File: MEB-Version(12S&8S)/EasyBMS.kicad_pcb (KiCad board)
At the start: 2 copper layers, 48.8 x 100 mm, 174 parts, among them IC1 XL7046, IC2 LTC6811IG-1#PBF, IC3 ISO1042DWV, IC4 AMS1117-3.3, J1 TYPE-C-31-M-12, Q14 CJ2301, Q15 CJ2301, Q16 CJ2301, Q18 CJ2301, Q20 CJ2301, Q22 CJ2301, Q24 CJ2301, Q26 CJ2301, Q28 CJ2301, Q30 CJ2301, Q32 CJ2301, Q34 CJ2301, U1 ESP32-C6-MINI-1-N4, Y1 FC-135_32.7680KA-A5

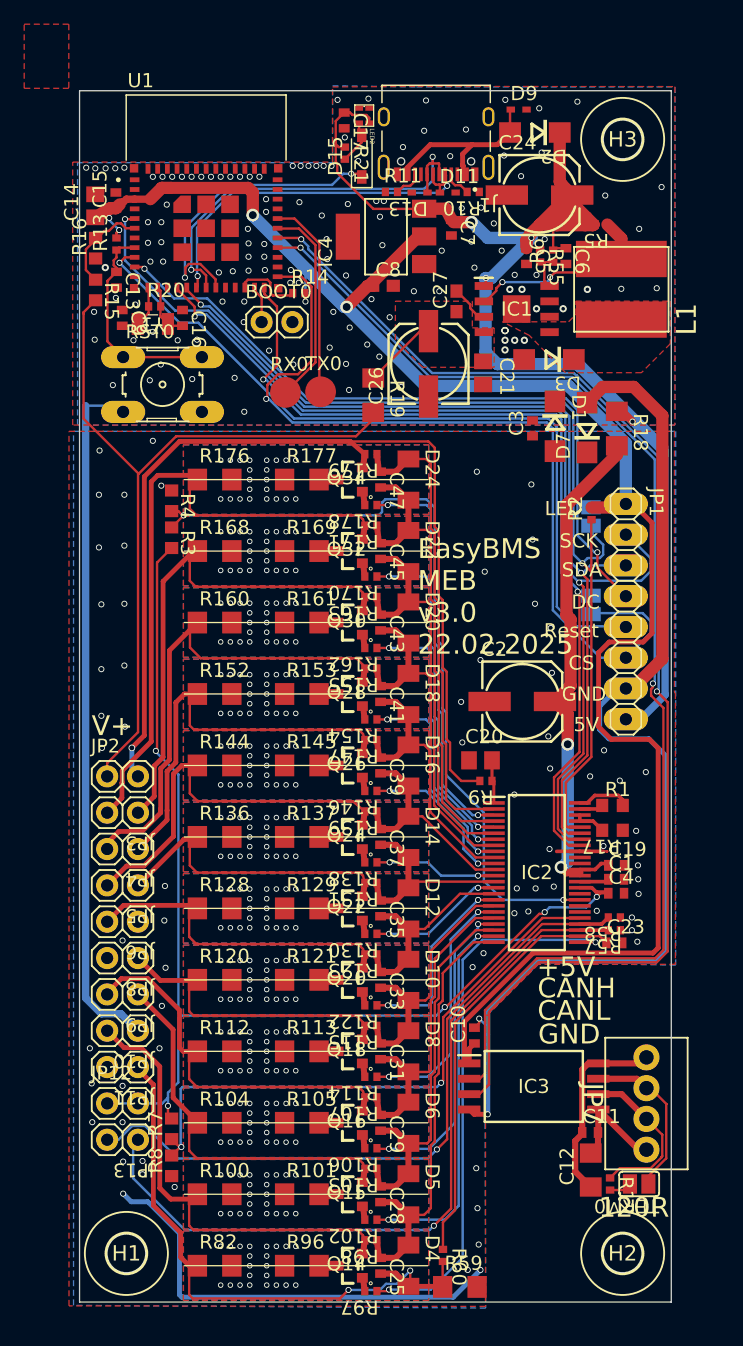
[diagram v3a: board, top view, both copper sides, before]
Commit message: new grounding with one common ground
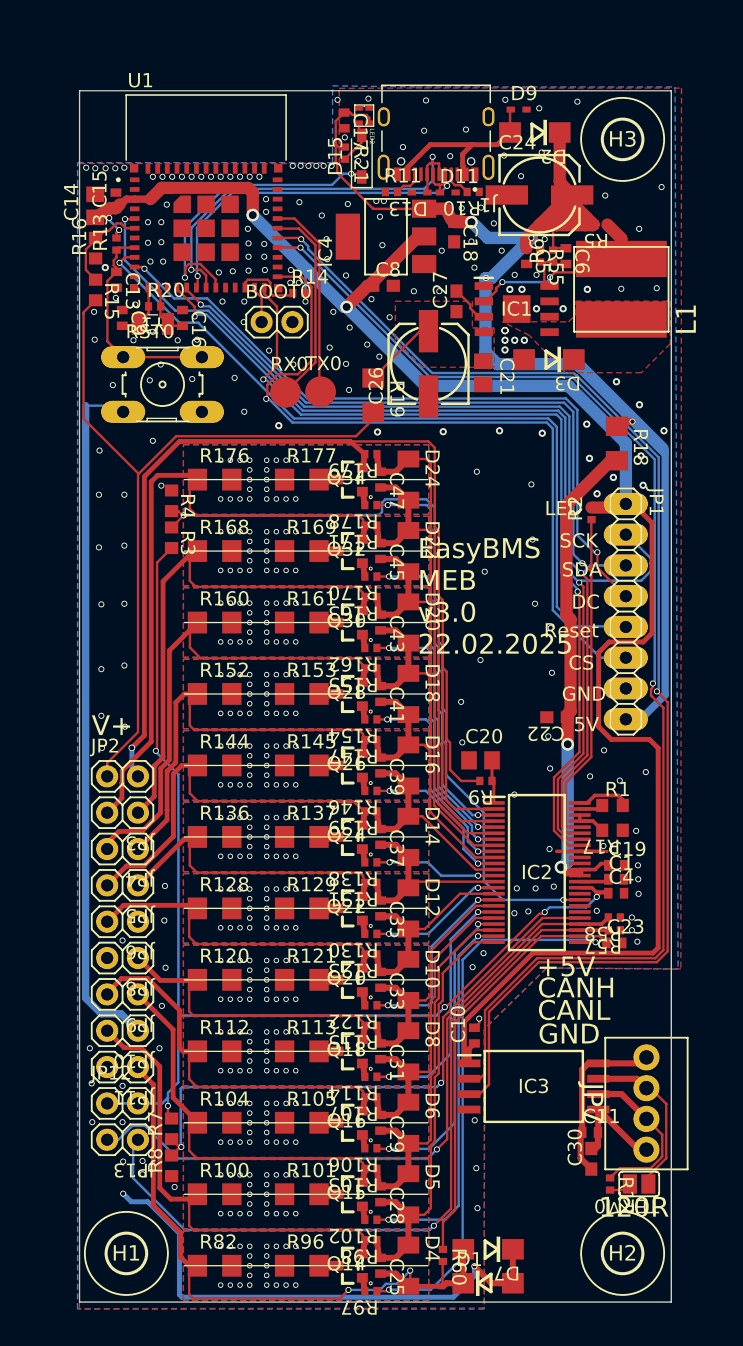
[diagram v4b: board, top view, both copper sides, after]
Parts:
- removed C12: 47µF, EasyBMS:C1206_334
- removed C2: 100µF/16V, EasyBMS:153CLV-0605_334
- removed C3: 100nF, EasyBMS:C0402_334
- removed C7: 1uF, EasyBMS:C0402_334
- removed CSLTC0, MISO0: SJ, EasyBMS:SJ_252
- removed R59: 600R@100MHz, EasyBMS:R1206_334
- added C18: 22uF, EasyBMS:C0603_334, F.Cu at (155.0, 66.6)
- added C22: 22uF, EasyBMS:C0603_334, F.Cu at (163.5, 106.7)
- added C30: 22uF, EasyBMS:C0603_334, F.Cu at (166.3, 143.2)
- moved D1 71.0 mm to (157.8, 153.4), turned to 0 degrees
- moved D7 68.3 mm to (157.8, 150.7), turned to 180 degrees
- moved R18 1.23 mm to (168.4, 84.1)
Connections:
- C1 pad 2: /GND2 -> GND
- C19 pad 2: /GND2 -> GND
- C20 pad 1: /GND2 -> GND
- C23 pad 2: /GND2 -> GND
- C4 pad 2: /GND2 -> GND
- D1 pad A: /GND2 -> GND
- D1 pad C: GND -> /C1-
- D7 pad A: GND -> /C1-
- D7 pad C: /GND2 -> GND
- IC2 pad 30: /GND2 -> GND
- IC2 pad 31: /GND2 -> GND
- IC2 pad 40: /GND2 -> GND
- R17 pad 1: /GND2 -> GND
- R4 pad 1: /GND2 -> GND
- R57 pad 1: /GND2 -> GND
- R58 pad 1: /GND2 -> GND
- R8 pad 1: /GND2 -> GND
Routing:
- net /GND2: track 41.1 -> 0.00 mm, vias 69 -> 0
- net GND: track 146.5 -> 108.4 mm, vias 129 -> 209
- net /CSDSPL: track 71.4 -> 62.3 mm
- net /C1-: track 49.8 -> 54.7 mm
- net /MISO: track 82.3 -> 77.5 mm
- net +5V: track 42.7 -> 40.9 mm
- net Net-(IC3-VCC2): track 16.2 -> 14.5 mm
- net /A0DSPL: track 60.0 -> 58.6 mm
- net /CSLTC: track 73.9 -> 72.6 mm
- net +5V/1: track 112.5 -> 112.2 mm, vias 4 -> 5
- removed copper zone on B.Cu, net /GND2
- removed copper zone on F.Cu, net /GND2

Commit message: add ESD protection to CAN, more clearance on high voltage diff
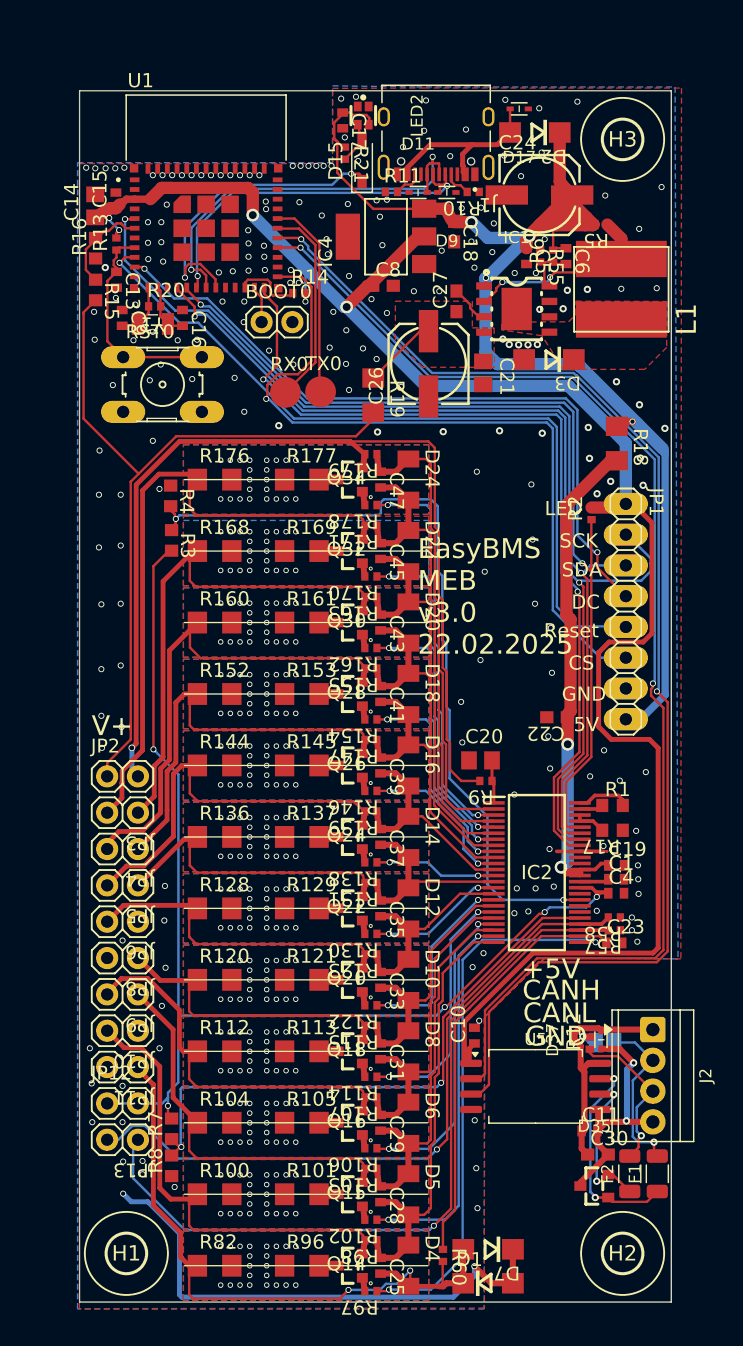
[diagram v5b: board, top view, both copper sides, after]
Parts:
- removed D13: LESD5D5.0CT1G, EasyBMS:SOD523_210
- removed IC3: ISO1042DWV, EasyBMS:SOIC127P1150X280-8N
- removed JP7: 2828XX-4282834-4, EasyBMS:TERMBLK_254-4N_16378166
- added D17: LESD5D5.0CT1G_C5199850, EasyEDA2KiCAD:SOD-523_L1.2-W0.8-LS1.6-BI, F.Cu at (160.4, 56.5)
- added D35: PESD1CAN,215, EasyEDA2KiCAD:SOT-23_L2.9-W1.3-P1.90-LS2.4-BR, F.Cu at (166.6, 145.4)
- added D37: LESD5D5.0CT1G_C5199850, EasyEDA2KiCAD:SOD-523_L1.2-W0.8-LS1.6-BI, F.Cu at (167.1, 133.3)
- added F1: 60V 100mA/JK-NSMD010, Resistor_SMD:R_1206_3216Metric, F.Cu at (171.8, 144.4)
- added F2: 60V 100mA/JK-NSMD010, Resistor_SMD:R_1206_3216Metric, F.Cu at (169.5, 144.4)
- added J2: Screw_Terminal_01x04, TerminalBlock_TE-Connectivity:TerminalBlock_TE_282834-4_1x04_P2.54mm_Horizontal, F.Cu at (171.4, 132.5)
- added U5: CA-IS3050CG, Package_SO:SOIC-8_7.5x5.85mm_P1.27mm, F.Cu at (161.7, 137.2)
- D11, D9: value LESD5D5.0CT1G -> LESD5D5.0CT1G_C5199850; footprint EasyBMS:SOD523_210 -> EasyEDA2KiCAD:SOD-523_L1.2-W0.8-LS1.6-BI
- IC1: footprint EasyBMS:SOIC127P600X170-9N -> EasyEDA2KiCAD:ESOP-8_L4.9-W3.9-P1.27-LS6.0-TL-EP
- LED2: footprint EasyBMS:XL-1615RGBC-WS2812B -> EasyEDA2KiCAD:LED-SMD_4P-L1.6-W1.5_XL-1615RGBC-WS2812B-1
- TERM0: moved to B.Cu
- moved TERM0 12.0 mm to (167.5, 133.6)
- moved R12 11.7 mm to (166.2, 133.6), turned to 90 degrees
- moved D9 9.02 mm to (154.4, 63.4), turned to 180 degrees
- moved D11 2.40 mm to (152.0, 63.4)
- moved C30 0.65 mm to (166.9, 142.8), turned to 0 degrees
- moved R4 0.41 mm to (131.6, 88.5)
- moved D15 0.39 mm to (147.4, 60.8)
- moved R3 0.22 mm to (131.7, 92.1)
- moved C11 0.14 mm to (166.2, 140.9)
- moved C17 0.13 mm to (145.8, 57.5)
- moved LED2 0.08 mm to (147.5, 57.1)
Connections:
- D2 pad A: Net-(D2-PadA) -> Net-(D17-Pad2)
- J1 pad A4_B9: Net-(D2-PadA) -> Net-(D17-Pad2)
- J1 pad B4_A9: Net-(D2-PadA) -> Net-(D17-Pad2)
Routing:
- net GND: track 108.4 -> 51.3 mm, vias 209 -> 208
- net Net-(U5-CANH): track 0.00 -> 17.6 mm, vias 0 -> 2
- net Net-(D2-PadA): track 15.0 -> 0.00 mm
- net Net-(D17-Pad2): track 0.00 -> 15.0 mm
- net Net-(U5-CANL): track 0.00 -> 12.4 mm, vias 0 -> 2
- net Net-(J2-Pin_4): track 9.02 -> 20.9 mm, vias 0 -> 2
- net Net-(J2-Pin_1): track 14.5 -> 19.4 mm
- net /VTEMPNORTH: track 65.7 -> 66.7 mm
- net Net-(R12-Pad2): track 1.85 -> 2.70 mm, vias 0 -> 1
- net Net-(J2-Pin_2): track 13.7 -> 14.2 mm, vias 0 -> 1
- net +5V/1: track 112.2 -> 111.7 mm, vias 5 -> 4
- net Net-(J2-Pin_3): track 13.5 -> 13.3 mm, vias 0 -> 1

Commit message: changed settings for jlc parts
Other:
- board text added: "EasyBMS MEB v3.1 19.05.2025"
- board text removed: "EasyBMS MEB v3.0 22.02.2025"
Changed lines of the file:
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@@
 		(sheetname "/")
 		(sheetfile "EasyBMS.kicad_sch")
-		(attr exclude_from_bom)
+		(attr exclude_from_pos_files exclude_from_bom)
 		(fp_poly
 			(pts
@@
 		(sheetname "/")
 		(sheetfile "EasyBMS.kicad_sch")
+		(attr exclude_from_pos_files exclude_from_bom)
 		(fp_line
 			(start 2.54 0.635)
@@
 		(sheetname "/")
 		(sheetfile "EasyBMS.kicad_sch")
-		(attr exclude_from_bom)
+		(attr exclude_from_pos_files exclude_from_bom)
 		(fp_poly
 			(pts
@@
 		(sheetname "/")
 		(sheetfile "EasyBMS.kicad_sch")
-		(attr exclude_from_bom)
+		(attr exclude_from_pos_files exclude_from_bom)
 		(fp_poly
 			(pts
@@
 		(sheetname "/")
 		(sheetfile "EasyBMS.kicad_sch")
-		(attr exclude_from_bom)
+		(attr exclude_from_pos_files exclude_from_bom)
 		(fp_poly
 			(pts
@@
 		(sheetname "/")
 		(sheetfile "EasyBMS.kicad_sch")
+		(attr exclude_from_pos_files exclude_from_bom)
 		(fp_line
 			(start 2.54 0.635)
@@
 		(sheetname "/")
 		(sheetfile "EasyBMS.kicad_sch")
+		(attr exclude_from_pos_files exclude_from_bom)
 		(fp_line
 			(start -2.54 -0.635)
@@
 		(sheetname "/")
 		(sheetfile "EasyBMS.kicad_sch")
-		(attr exclude_from_bom)
+		(attr exclude_from_pos_files exclude_from_bom)
 		(fp_poly
 			(pts
@@
 		(sheetname "/")
 		(sheetfile "EasyBMS.kicad_sch")
+		(attr exclude_from_pos_files exclude_from_bom)
 		(fp_line
 			(start 2.54 0.635)
@@
 		(sheetname "/")
 		(sheetfile "EasyBMS.kicad_sch")
-		(attr exclude_from_bom)
+		(attr exclude_from_pos_files exclude_from_bom)
 		(fp_poly
 			(pts
@@
 		(sheetname "/")
 		(sheetfile "EasyBMS.kicad_sch")
+		(attr exclude_from_pos_files exclude_from_bom)
 		(fp_line
 			(start 2.54 0.635)
@@
 		(sheetname "/")
 		(sheetfile "EasyBMS.kicad_sch")
-		(attr exclude_from_bom)
+		(attr exclude_from_pos_files exclude_from_bom)
 		(fp_poly
 			(pts
@@
 		(sheetname "/")
 		(sheetfile "EasyBMS.kicad_sch")
+		(attr exclude_from_pos_files exclude_from_bom)
 		(fp_line
 			(start 2.54 0.635)
@@
 		(sheetname "/")
 		(sheetfile "EasyBMS.kicad_sch")
-		(attr exclude_from_bom)
+		(attr exclude_from_pos_files exclude_from_bom)
 		(fp_poly
 			(pts
@@
 		(sheetname "/")
 		(sheetfile "EasyBMS.kicad_sch")
+		(attr exclude_from_pos_files exclude_from_bom)
 		(fp_line
 			(start -2.54 -0.635)
@@
 		(sheetname "/")
 		(sheetfile "EasyBMS.kicad_sch")
-		(attr exclude_from_bom)
+		(attr exclude_from_pos_files exclude_from_bom)
 		(fp_poly
 			(pts
@@
 		(sheetname "/")
 		(sheetfile "EasyBMS.kicad_sch")
-		(attr exclude_from_pos_files exclude_from_bom)
+		(attr exclude_from_bom)
 		(fp_line
 			(start -2.54 -0.635)
@@
 		(sheetname "/")
 		(sheetfile "EasyBMS.kicad_sch")
-		(attr exclude_from_bom)
+		(attr exclude_from_pos_files exclude_from_bom)
 		(fp_poly
 			(pts
@@
 		(sheetname "/")
 		(sheetfile "EasyBMS.kicad_sch")
+		(attr exclude_from_pos_files exclude_from_bom)
 		(fp_line
 			(start 2.54 0.635)
@@
 		(sheetname "/")
 		(sheetfile "EasyBMS.kicad_sch")
-		(attr exclude_from_bom)
+		(attr exclude_from_pos_files exclude_from_bom)
 		(fp_poly
 			(pts
@@
 		(sheetname "/")
 		(sheetfile "EasyBMS.kicad_sch")
+		(attr exclude_from_pos_files exclude_from_bom)
 		(fp_line
 			(start 2.54 0.635)
@@
 		(sheetname "/")
 		(sheetfile "EasyBMS.kicad_sch")
-		(attr exclude_from_bom)
+		(attr exclude_from_pos_files exclude_from_bom)
 		(fp_poly
 			(pts
@@
 		(sheetname "/")
 		(sheetfile "EasyBMS.kicad_sch")
+		(attr exclude_from_pos_files exclude_from_bom)
 		(fp_line
 			(start 2.54 0.635)
@@
 		(sheetname "/")
 		(sheetfile "EasyBMS.kicad_sch")
+		(attr exclude_from_pos_files exclude_from_bom)
 		(fp_line
 			(start 2.54 0.635)
@@
 		(layer "F.Fab")
 	)
-	(gr_text "EasyBMS\nMEB\nv3.0\n22.02.2025"
+	(gr_text "EasyBMS\nMEB\nv3.1\n19.05.2025"
 		(at 151.9907 101.6748 0)
 		(layer "F.SilkS")
@@
 			(pts
 				(xy 172.5523 76.185163) (xy 170.732663 78.0048) (xy 164.024456 78.0048) (xy 162.25 75.225) (xy 158.925 74.75)
-				(xy 158.925 74.1) (xy 164.4499 74.0774) (xy 165.0499 73.4774) (xy 165.0499 72.3774) (xy 172.55 72.4)
+				(xy 158.925 74.225714) (xy 164.323669 74.203631) (xy 165.0499 73.4774) (xy 165.0499 72.3774) (xy 172.55 72.4)
 			)
 		)

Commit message: changed RGB LED and new simple red LED
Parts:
- removed LED2: XL-1615RGBC-WS2812B, EasyEDA2KiCAD:LED-SMD_4P-L1.6-W1.5_XL-1615RGBC-WS2812B-1
- added D13: LED, LED_SMD:LED_0603_1608Metric, F.Cu at (136.1, 74.5)
- added R22: 1k, EasyBMS:R0402_334, F.Cu at (134.9, 73.2)
- added U2: XL-0807RGBC-WS2812B, EasyEDA2KiCAD:LED-SMD_4P-L2.0-W1.8_XL-0807RGBC-WS2812B, F.Cu at (147.4, 57.0)
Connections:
- U1 pad 20: unconnected-(U1-IO15-Pad20) -> /LED
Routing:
- net /LED: track 0.00 -> 1.96 mm
- net Net-(D13-A): track 0.00 -> 1.22 mm
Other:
- board text added: "EasyBMS MEB v3.2 30.09.2025"
- board text removed: "EasyBMS MEB v3.1 19.05.2025"

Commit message: replace old imported symbols and footprints with kicad ones
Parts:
- removed IC1: XL7046, EasyEDA2KiCAD:ESOP-8_L4.9-W3.9-P1.27-LS6.0-TL-EP
- removed IC2: LTC6811IG-1#PBF, EasyBMS:SOP50P780X200-48N
- removed L1: 100µH, EasyBMS:CY75-100UH
- added L2: 100µH, EasyEDA2KiCAD:IND-SMD_L7.8-W7.0-A, F.Cu at (168.8, 71.2)
- added U3: LTC6811-1, Package_SO:SSOP-48_5.3x12.8mm_P0.5mm, F.Cu at (161.9, 119.5)
- added U4: XL7046, EasyEDA2KiCAD:ESOP-8_L4.9-W3.9-P1.27-LS6.0-TL-EP, F.Cu at (160.2, 73.1)
- BOOT0, JP10, JP11, JP12, JP13, JP2, JP3, JP4, JP5, JP6, JP8, JP9: footprint EasyBMS:1X02 -> Connector_PinHeader_2.54mm:PinHeader_1x02_P2.54mm_Vertical
- C1, C10, C11, C13, C15, C16, C17, C19, C23, C25, C28, C29, C31, C33, C35, C37, C39, C4, C41, C43, C45, C47, C5, C6, C9: footprint EasyBMS:C0402_334 -> Capacitor_SMD:C_0402_1005Metric
- C14, C20, C21: footprint EasyBMS:C0805_334 -> Capacitor_SMD:C_0805_2012Metric
- C18, C22, C27, C30, C8: footprint EasyBMS:C0603_334 -> Capacitor_SMD:C_0603_1608Metric
- C24: footprint EasyBMS:153CLV-0605_334 -> Capacitor_SMD:CP_Elec_6.3x5.4
- C26: footprint EasyBMS:153CLV-0605_334 -> Capacitor_SMD:CP_Elec_6.3x7.7
- D1, D2, D3, D7: footprint EasyBMS:DO214AC_210 -> Diode_SMD:D_SMA
- D10, D12, D14, D16, D18, D20, D22, D24, D4, D5, D6, D8: footprint EasyBMS:MELF-MLL34 -> Diode_SMD:D_MiniMELF
- D11, D17, D37, D9: footprint EasyEDA2KiCAD:SOD-523_L1.2-W0.8-LS1.6-BI -> Diode_SMD:D_SOD-523
- D15: footprint EasyBMS:SOD3715X135_16378169 -> Diode_SMD:D_SOD-123
- D35: footprint EasyEDA2KiCAD:SOT-23_L2.9-W1.3-P1.90-LS2.4-BR -> Package_TO_SOT_SMD:SOT-23
- IC4: footprint EasyBMS:SOT223_111 -> Package_TO_SOT_SMD:SOT-223-3_TabPin2
- J1: footprint EasyBMS:HRO_TYPE-C-31-M-12 -> Connector_USB:USB_C_Receptacle_HRO_TYPE-C-31-M-12
- JP1: footprint EasyBMS:1X08_16378166 -> Connector_PinHeader_2.54mm:PinHeader_1x08_P2.54mm_Vertical
- Q14, Q15, Q16, Q18, Q20, Q22, Q24, Q26, Q28, Q30, Q32, Q34: footprint EasyBMS:PG-SOT-23 -> Package_TO_SOT_SMD:SOT-23
- R1, R15, R16, R17, R3, R4, R7, R8: footprint EasyBMS:R0603_334 -> Resistor_SMD:R_0603_1608Metric
- R10, R102, R103, R106, R107, R11, R114, R115, R12, R122, R123, R13, R130, R131, R138, R139, R14, R146, R147, R154, R155, R162, R163, R170, R171, R178, R179, R2, R20, R21, R22, R5, R55, R57, R58, R6, R60, R9, R97, R98: footprint EasyBMS:R0402_334 -> Resistor_SMD:R_0402_1005Metric
- R100, R101, R104, R105, R112, R113, R120, R121, R128, R129, R136, R137, R144, R145, R152, R153, R160, R161, R168, R169, R176, R177, R18, R19, R82, R96: footprint EasyBMS:R1206_334 -> Resistor_SMD:R_1206_3216Metric
- RST0: footprint EasyBMS:B3F-10XX_377 -> Button_Switch_THT:SW_PUSH_6mm
- RX0, TX0: footprint EasyBMS:B2,54_385 -> TestPoint:TestPoint_Pad_D2.0mm
- TERM0: footprint EasyBMS:SJ_252 -> Jumper:SolderJumper-2_P1.3mm_Open_RoundedPad1.0x1.5mm
- U1: value ESP32-C6-MINI-1-N4 -> ESP32-C6-MINI-1; footprint EasyBMS:XCVR_ESP32-C6-MINI-1-N4 -> RF_Module:ESP32-C6-MINI-1
- Y1: footprint EasyBMS:FC135327680KAA5 -> EasyEDA2KiCAD:FC-135R_L3.2-W1.5
- moved JP1 8.94 mm to (169.3, 89.1), turned to 0 degrees
- moved C17 7.06 mm to (144.2, 64.3), turned to 0 degrees
- moved U2 6.83 mm to (143.6, 62.7), turned to 180 degrees
- moved R21 5.53 mm to (142.3, 64.3), turned to 180 degrees
- moved RST0 4.37 mm to (134.3, 82.0), turned to 180 degrees
- moved D15 2.63 mm to (146.2, 63.1)
- moved JP3 1.32 mm to (128.9, 114.6), turned to -90 degrees
- moved JP10 1.31 mm to (128.9, 132.6), turned to -90 degrees
- moved JP11 1.31 mm to (128.9, 135.6), turned to -90 degrees
- moved JP12 1.31 mm to (128.9, 138.6), turned to -90 degrees
- moved JP13 1.31 mm to (128.9, 141.6), turned to -90 degrees
- moved JP4 1.31 mm to (128.9, 117.6), turned to -90 degrees
- moved JP5 1.31 mm to (128.9, 120.6), turned to -90 degrees
- moved JP6 1.31 mm to (128.9, 123.6), turned to -90 degrees
- moved JP8 1.31 mm to (128.9, 126.6), turned to -90 degrees
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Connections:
- net /V+ renamed Net-(U3-V+)
- BOOT0 pad 1: Net-(U1-IO9) -> GND
- BOOT0 pad 2: GND -> Net-(BOOT0-B)
- C13 pad 1: Net-(RST0-S) -> Net-(U1-EN)
- C21 pad 1: Net-(IC1-VIN) -> Net-(U4-VIN)
- C27 pad 1: Net-(IC1-VIN) -> Net-(U4-VIN)
- D17 pad 2: Net-(D17-Pad2) -> Net-(D2-A)
- J1 pad A8: unconnected-(J1-SBU1-PadA8) -> (no net)
- J1 pad B8: unconnected-(J1-SBU2-PadB8) -> (no net)
- R13 pad 1: Net-(RST0-S) -> Net-(U1-EN)
- R19 pad 1: Net-(IC1-VIN) -> Net-(U4-VIN)
- RST0 pad 1: Net-(RST0-S) -> GND
- RST0 pad 2: Net-(RST0-S) -> Net-(U1-EN)
- U1 pad 23: Net-(U1-IO9) -> Net-(BOOT0-B)
- U1 pad 8: Net-(RST0-S) -> Net-(U1-EN)
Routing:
- net Net-(D2-A): track 0.00 -> 20.6 mm, vias 0 -> 3
- net Net-(U1-EN): track 0.00 -> 18.6 mm
- net Net-(RST0-S): track 18.0 -> 0.00 mm
- net Net-(D17-Pad2): track 15.0 -> 0.00 mm
- net Net-(U4-VIN): track 0.00 -> 6.16 mm
- net Net-(IC1-VIN): track 6.16 -> 0.00 mm
- net +5V/1: track 111.9 -> 105.8 mm, vias 4 -> 7
- net Net-(D15-A): track 3.55 -> 6.65 mm, vias 0 -> 2
- net Net-(U1-IO9): track 3.09 -> 0.00 mm
- net Net-(BOOT0-B): track 0.00 -> 3.09 mm
- net /D+: track 34.1 -> 31.7 mm
- net GND: track 51.3 -> 49.3 mm, vias 208 -> 199
- net Net-(J1-CC1): track 2.26 -> 3.19 mm
- net Net-(J1-CC2): track 2.37 -> 3.16 mm
- net /LEDDATA: track 25.4 -> 26.0 mm
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- added copper zone on F.Cu, net Net-(D3-K)
- added copper zone on F.Cu, net Net-(U4-VIN)
- removed copper zone on F.Cu, net Net-(IC1-VIN)
- removed copper zone on F.Cu, net Net-(L1-1)
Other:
- board text added: "EasyBMS MEB v3.3 06.11.2025"
- board text removed: "EasyBMS MEB v3.2 30.09.2025"
